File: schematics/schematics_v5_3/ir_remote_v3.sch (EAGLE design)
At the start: 27 parts, among them IC1 AP1117E50G, Q1 10MHz, T11 TASTER3301, T12 TASTER3301, T13 TASTER3301, T14 TASTER3301, T15 TASTER3301

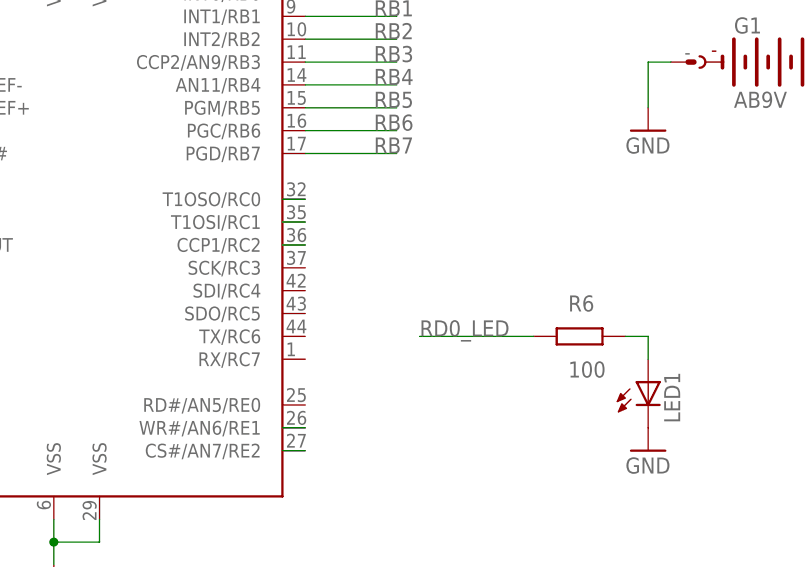
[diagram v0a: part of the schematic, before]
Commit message: Add minor modifications including ground and battery areas
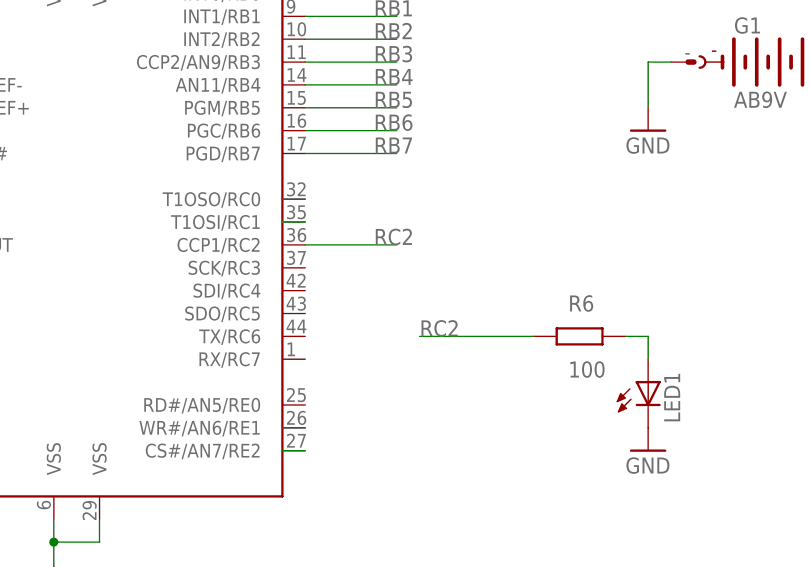
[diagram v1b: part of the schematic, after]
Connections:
- removed net RDS_INT: IC8.CCP1/RC2
- new net RC2: IC8.CCP1/RC2, R6.1
- net RD0_LED: no longer R6.1
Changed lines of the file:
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@@
 <?xml version="1.0" encoding="utf-8"?>
 <!DOCTYPE eagle SYSTEM "eagle.dtd">
-<eagle version="8.3.1">
+<eagle version="9.6.2">
 <drawing>
 <settings>
@@
 </segment>
 </net>
-<net name="RDS_INT" class="0">
-<segment>
-<wire x1="127" y1="129.54" x2="129.54" y2="129.54" width="0.1524" layer="91"/>
+<net name="RC2" class="0">
+<segment>
 <pinref part="IC8" gate="G$1" pin="CCP1/RC2"/>
+<wire x1="129.54" y1="129.54" x2="139.7" y2="129.54" width="0.1524" layer="91"/>
+<label x="137.16" y="129.54" size="1.778" layer="95"/>
+</segment>
+<segment>
+<wire x1="142.24" y1="119.38" x2="154.94" y2="119.38" width="0.1524" layer="91"/>
+<label x="142.24" y="119.38" size="1.778" layer="95"/>
+<pinref part="R6" gate="G$1" pin="1"/>
 </segment>
 </net>
@@
 <label x="66.04" y="124.46" size="1.778" layer="95"/>
 </segment>
-<segment>
-<wire x1="142.24" y1="119.38" x2="154.94" y2="119.38" width="0.1524" layer="91"/>
-<label x="142.24" y="119.38" size="1.778" layer="95"/>
-<pinref part="R6" gate="G$1" pin="1"/>
-</segment>
-</net>
+</net>

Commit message: Add minor changes to layout v5_3
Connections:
- removed net RD0_LED: IC8.RD0/PSP0
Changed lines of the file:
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@@
 <?xml version="1.0" encoding="utf-8"?>
 <!DOCTYPE eagle SYSTEM "eagle.dtd">
-<eagle version="9.6.2">
+<eagle version="8.3.1">
 <drawing>
 <settings>
@@
 </segment>
 </net>
-<net name="RD0_LED" class="0">
-<segment>
-<pinref part="IC8" gate="G$1" pin="RD0/PSP0"/>
-<wire x1="78.74" y1="124.46" x2="66.04" y2="124.46" width="0.1524" layer="91"/>
-<label x="66.04" y="124.46" size="1.778" layer="95"/>
-</segment>
-</net>

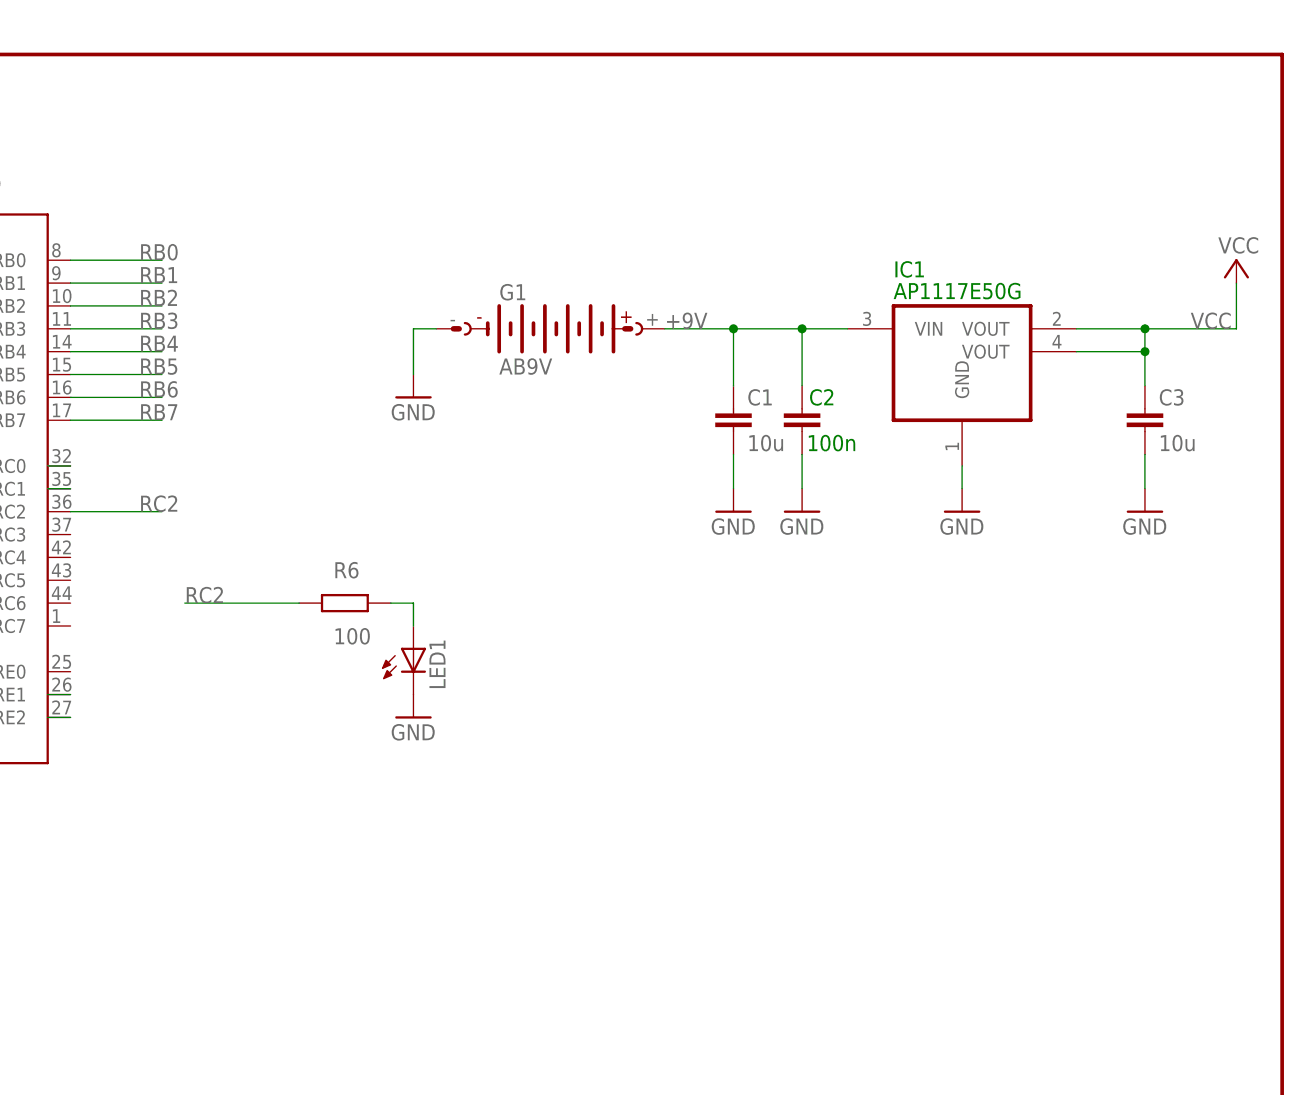
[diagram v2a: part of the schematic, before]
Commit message: Add pwm
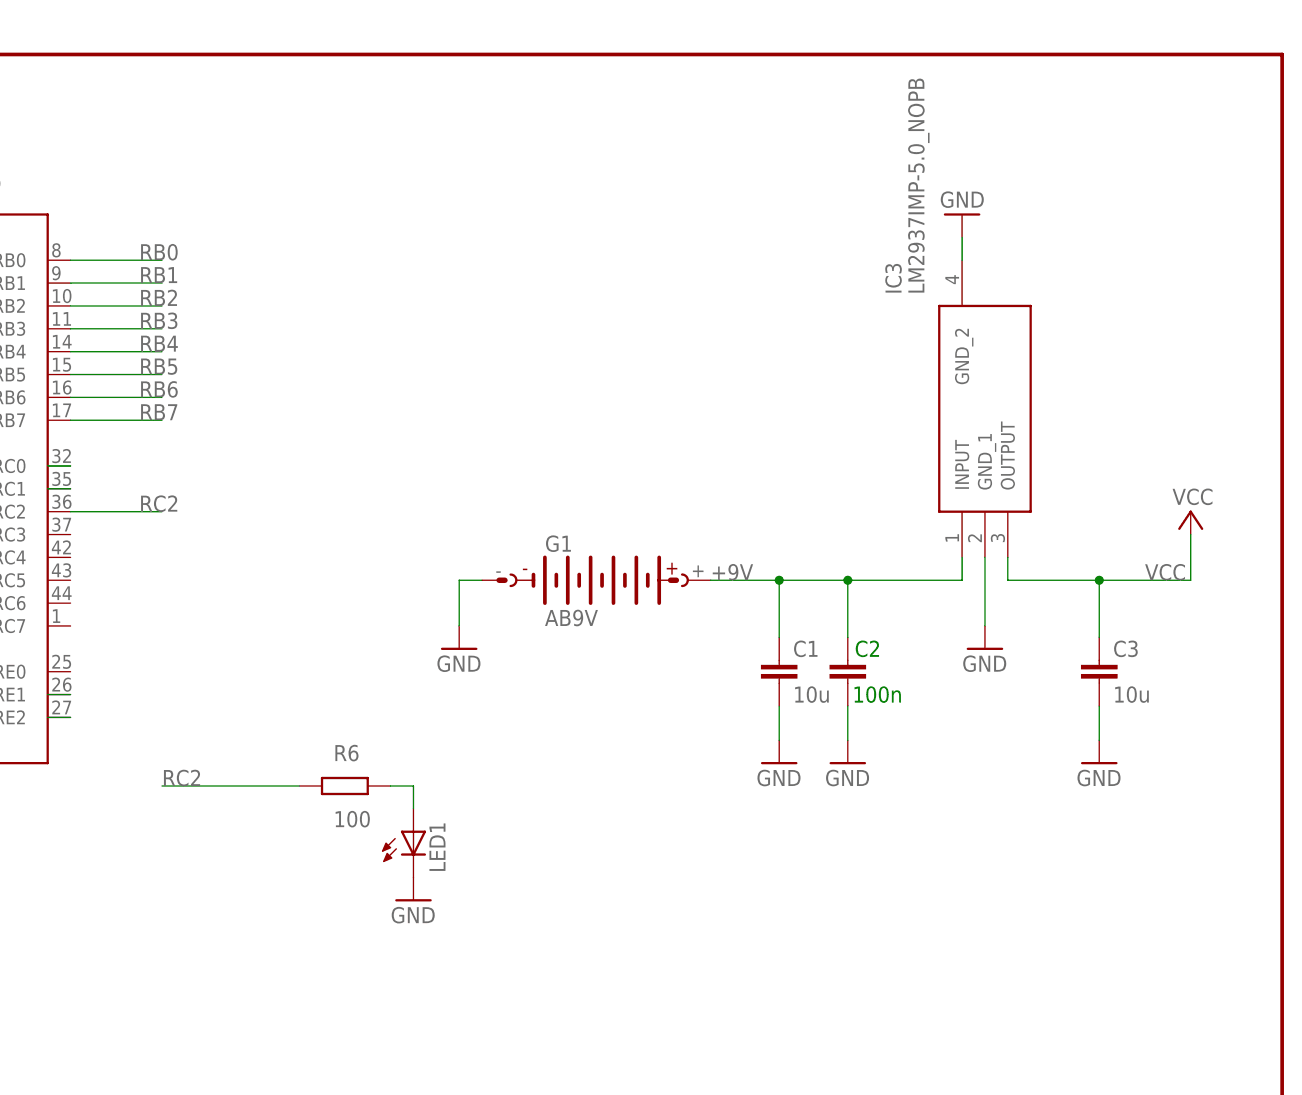
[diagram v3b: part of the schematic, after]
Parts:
- removed IC1: AP1117E50G, Bernd_110428:REG1117-2OUT
- added IC3: LM2937IMP-5.0_NOPB, LM2937IMP-5.0_NOPB:LM2937IMP-5.0_NOPB
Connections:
- net +9V: now also IC3.INPUT; no longer IC1.VIN
- net GND: now also IC3.GND_1, IC3.GND_2; no longer IC1.GND
- net VCC: now also IC3.OUTPUT; no longer IC1.VOUT, IC1.VOUT@1
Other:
- moved on the sheet: C1, C2, C3, G1, LED1, R6
